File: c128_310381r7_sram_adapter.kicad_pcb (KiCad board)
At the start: 2 copper layers, 20 parts, among them J1 T_0_L_DRAM, J10 T_6_L_DRAM, J2 L_0_L_DRAM, J3 T_7_R_DRAM, J4 L_7_R_DRAM, J5 T_1_L_DRAM, J6 T_2_L_DRAM, J7 T_3_L_DRAM, J8 T_4_L_DRAM, J9 T_5_L_DRAM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

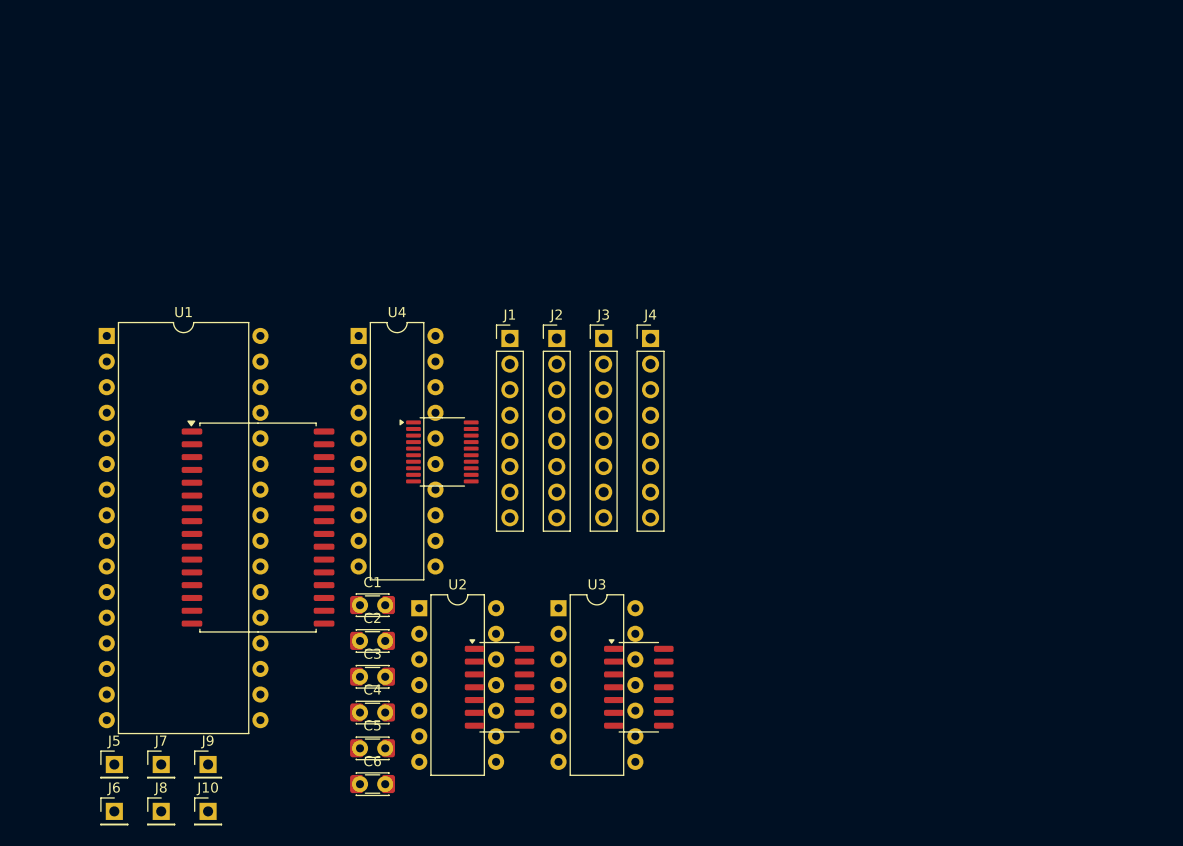
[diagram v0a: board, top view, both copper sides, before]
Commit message: Begin drawing traces
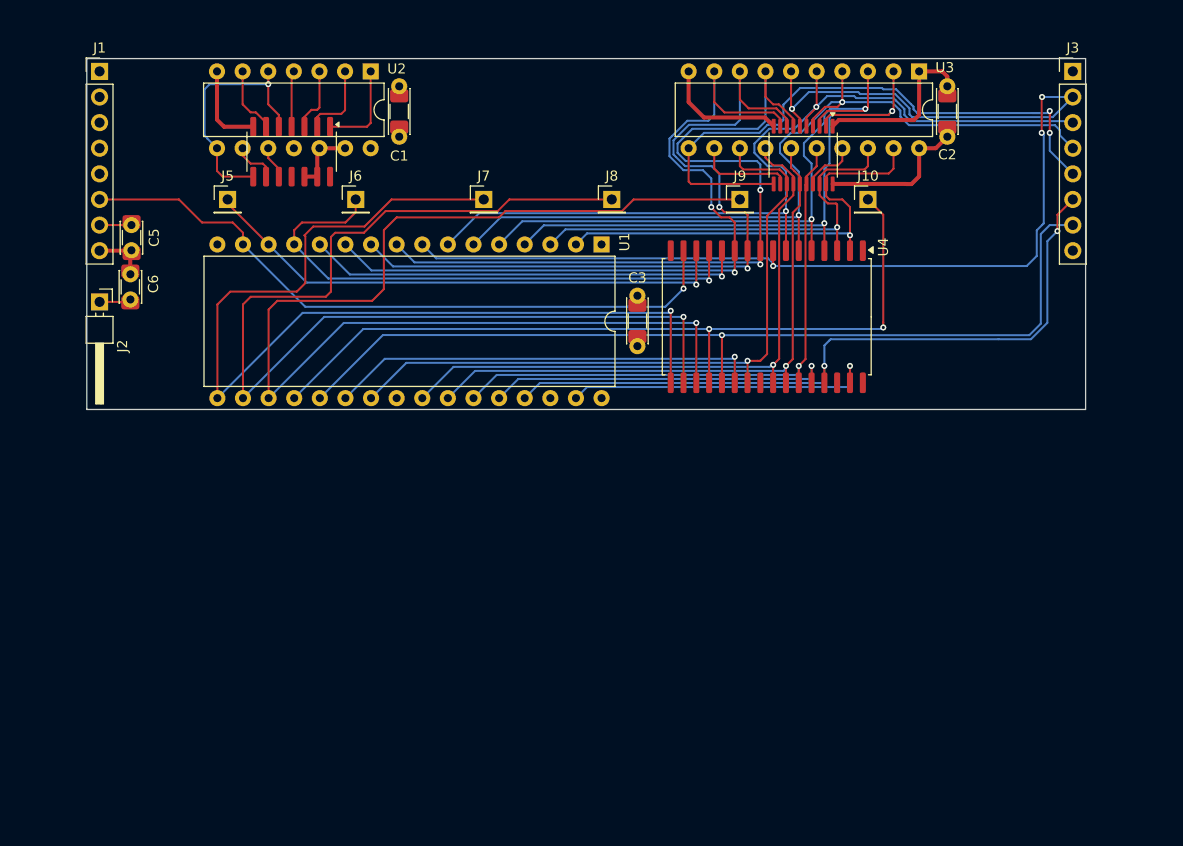
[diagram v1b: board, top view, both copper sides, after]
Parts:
- removed C4: 100nF, DoubleFootprint_Library:C_Disc_1206
- removed J4: L_7_R_DRAM, Connector_PinHeader_2.54mm:PinHeader_1x08_P2.54mm_Vertical
- removed the U3 at (121.7, 81.2)
- added U4: 128K x 8 SRAM, Package_SO:SOP-32_11.305x20.495mm_P1.27mm, F.Cu at (142.4, 52.3)
- C1, C2, C3: footprint DoubleFootprint_Library:C_Disc_1206 -> DoubleFootprint_Library:C_Disc_1206_P5.00mm
- C5, C6: footprint DoubleFootprint_Library:C_Disc_1206 -> DoubleFootprint_Library:C_Disc_1206_P2.50mm
- J2: value L_0_L_DRAM -> 2nd CAS; footprint Connector_PinHeader_2.54mm:PinHeader_1x08_P2.54mm_Vertical -> Connector_PinHeader_2.54mm:PinHeader_1x01_P2.54mm_Horizontal
- U1: footprint DoubleFootprint_Library:DIP-SOP-32 -> Package_DIP:DIP-32_W15.24mm
- U2: value 74HCT32 -> 74HCT00
- moved J10 89.2 mm to (152.4, 40.6)
- moved J9 77.0 mm to (139.7, 40.6)
- moved C2 76.8 mm to (160.3, 34.4), turned to 90 degrees
- moved J8 75.4 mm to (127.0, 40.6)
- moved J6 65.2 mm to (101.6, 40.6)
- moved J7 64.5 mm to (114.3, 40.6)
- moved U3 61.5 mm to (157.5, 27.9), turned to -90 degrees
- moved J5 57.2 mm to (88.9, 40.6)
- moved C5 56.6 mm to (79.4, 43.2), turned to -90 degrees
- moved J3 53.5 mm to (172.7, 27.9)
- moved U2 53.5 mm to (103.1, 27.9), turned to -90 degrees
- moved C6 53.2 mm to (79.3, 50.6), turned to 90 degrees
- moved U1 49.9 mm to (126.0, 45.1), turned to -90 degrees
- moved J1 48.6 mm to (76.2, 27.9)
- moved C1 46.6 mm to (105.9, 34.4), turned to 90 degrees
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- renumbered U4 to U3
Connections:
- J1 pad 6: /D0 -> /D2
- J2 pad 1: unconnected-(J2-Pin_1-Pad1) -> /~{CAS_B}
- J3 pad 2: /MA1 -> /MA0
- J3 pad 3: /MA2 -> /MA1
- J3 pad 4: /MA0 -> /MA2
- J6 pad 1: /D2 -> /D0
- U1 pad 23: /A4 -> /A5
- U1 pad 25: /A5 -> /A4
- U2 pad 1: /~{CAS_A} -> /~{CAS_B}
- U2 pad 10: GND -> /~{RAS}
- U2 pad 2: /~{RAS} -> /~{CAS_A}
- U2 pad 3: /~{SRAM_EN_A} -> /CAS
- U2 pad 4: /~{CAS_B} -> /CAS
- U2 pad 5: /~{RAS} -> /RAS
- U2 pad 6: /~{SRAM_EN_B} -> /~{SRAM_EN}
- U2 pad 8: unconnected-(U2-Pad8)_1 -> /RAS
- U2 pad 9: GND -> /~{RAS}
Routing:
- net /MA0: track 0.00 -> 119.7 mm, vias 0 -> 4
- net /D5: track 0.00 -> 114.9 mm, vias 0 -> 1
- net /D4: track 0.00 -> 106.9 mm, vias 0 -> 1
- net /D3: track 0.00 -> 98.6 mm, vias 0 -> 1
- net /D7: track 0.00 -> 92.2 mm, vias 0 -> 1
- net /MA1: track 0.00 -> 88.4 mm, vias 0 -> 2
- net /MA2: track 0.00 -> 85.5 mm, vias 0 -> 2
- net /D6: track 0.00 -> 80.0 mm, vias 0 -> 2
- net /MA6: track 0.00 -> 78.2 mm, vias 0 -> 2
- net /MA5: track 0.00 -> 78.1 mm, vias 0 -> 2
- net /MA4: track 0.00 -> 77.9 mm, vias 0 -> 2
- net /~{W}: track 0.00 -> 72.0 mm, vias 0 -> 2
- net /A5: track 0.00 -> 68.5 mm, vias 0 -> 1
- net /~{RAS}: track 0.00 -> 68.2 mm, vias 0 -> 2
- net /D2: track 0.00 -> 67.5 mm, vias 0 -> 1
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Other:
- board outline added: 99.1 x 34.8 mm

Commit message: Complete routing of first revision of the adapter
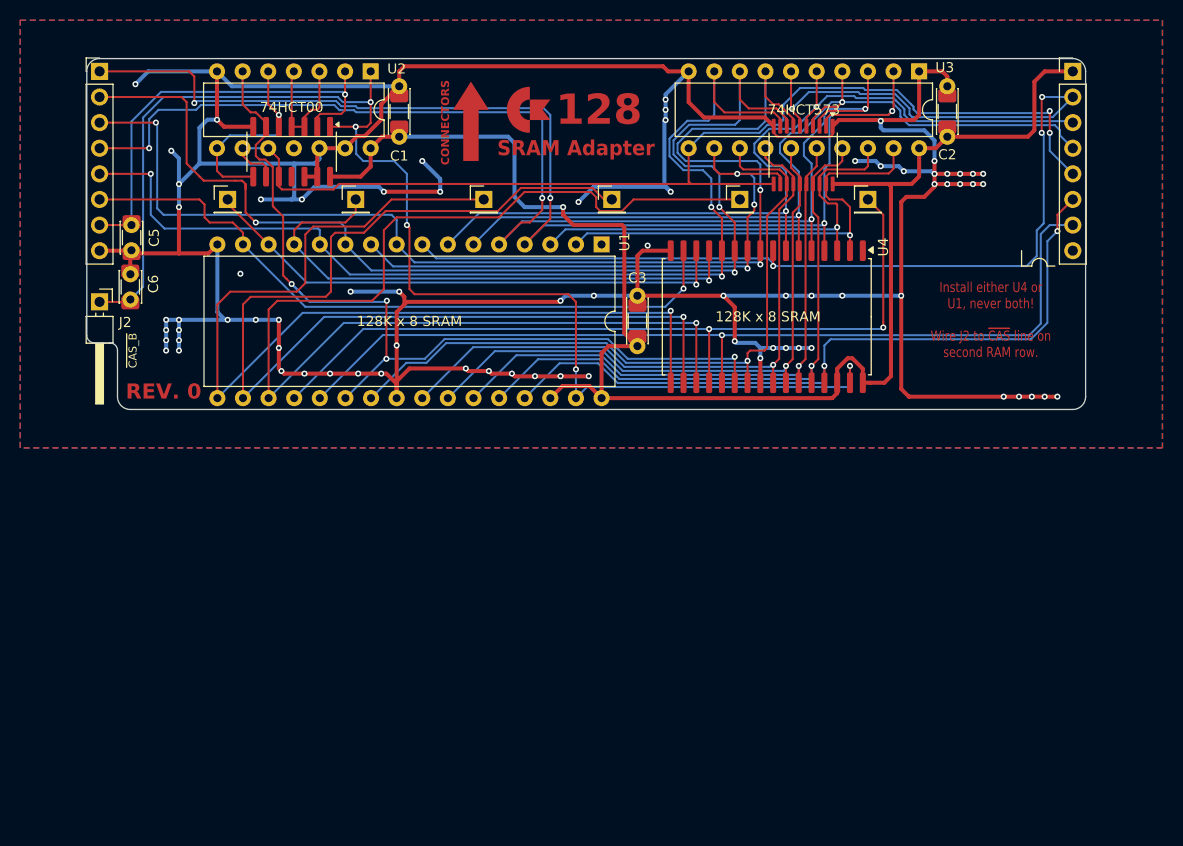
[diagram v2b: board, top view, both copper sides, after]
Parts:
- J2: value 2nd CAS -> ~{CAS_B}
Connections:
- U1 pad 10: /MA5 -> /A6
- U1 pad 11: /MA6 -> /MA5
- U1 pad 12: /A6 -> /MA6
- U1 pad 31: /~{CAS_A} -> /~{CAS_B}
- U4 pad 10: /MA5 -> /A6
- U4 pad 11: /MA6 -> /MA5
- U4 pad 12: /A6 -> /MA6
- U4 pad 31: /~{CAS_A} -> /~{CAS_B}
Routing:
- net GND: track 50.2 -> 434.9 mm, vias 0 -> 76
- net VCC: track 15.0 -> 151.8 mm, vias 0 -> 1
- net /~{CAS_B}: track 12.5 -> 132.7 mm, vias 0 -> 5
- net /MA3: track 60.5 -> 123.2 mm, vias 2 -> 4
- net /MA7: track 62.2 -> 124.3 mm, vias 2 -> 4
- net /~{RAS}: track 68.2 -> 112.9 mm
- net /MA4: track 77.9 -> 118.8 mm, vias 2 -> 3
- net /MA5: track 78.1 -> 115.3 mm, vias 2 -> 3
- net /~{SRAM_EN}: track 49.7 -> 86.7 mm, vias 1 -> 4
- net /MA6: track 78.2 -> 106.9 mm, vias 2 -> 3
- net /A2: track 40.2 -> 60.4 mm
- net /A6: track 53.4 -> 59.2 mm, vias 1 -> 3
- net /RAS: track 24.9 -> 20.5 mm
- net /D5: track 114.9 -> 117.0 mm
- net /A5: track 68.5 -> 70.3 mm
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- added copper zone on B.Cu, net GND
- added copper zone on F.Cu, net GND
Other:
- outline, holes or cut-outs redrawn
- board text added: "128"
- board text added: "CONNECTORS"
- board text added: "Install either U4 or U1, never both! Wire J2 to ~{CAS} line on second RAM row."
- board text added: "REV. 0"
- board text added: "SRAM Adapter"

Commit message: Update silkscreen and drawings on the PCB
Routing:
- net GND: track 434.9 -> 456.3 mm, vias 76 -> 84
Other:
- board text added: "Install either U4 or U1, never both! Wire J2 to ~{CAS} on U38, pin 15."
- board text added: "U38"
- board text removed: "Install either U4 or U1, never both! Wire J2 to ~{CAS} line on second RAM row."
